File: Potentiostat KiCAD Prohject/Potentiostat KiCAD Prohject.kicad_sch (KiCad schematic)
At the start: 45 parts, among them J2 USB_C_Receptacle_USB2.0, K1 DIPxx-1Axx-12xD, SW1 Reset, SW2 Boot, U1 OPA2277, U10 ADS1115IDGS, U11 MCP4725xxx-xCH, U13 LD1117S33TR_SOT223, U14 ESP32-S2-SOLO, U2 TL074, U4 OPA2277, U5 INA128, U6 MCP4725xxx-xCH, U7 INA128, U8 REF3033, U9 INA128

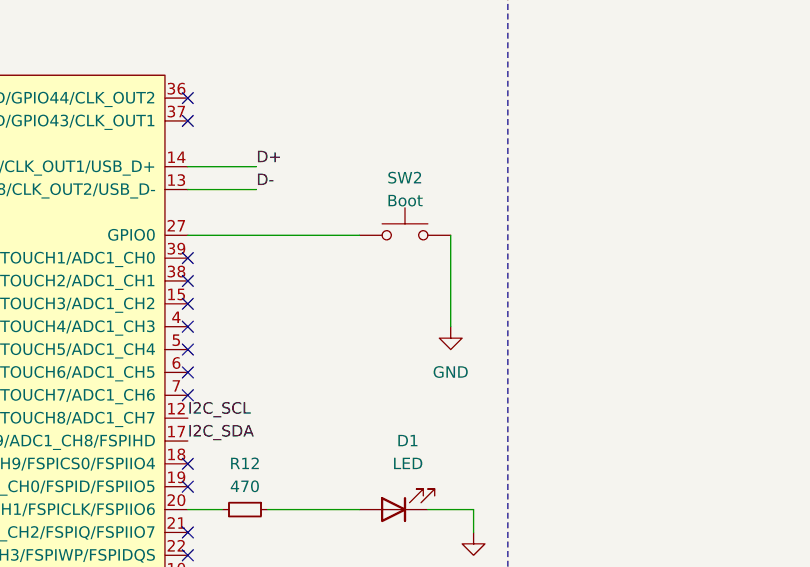
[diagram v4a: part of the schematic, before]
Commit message: Changed resistors and assigned footprints
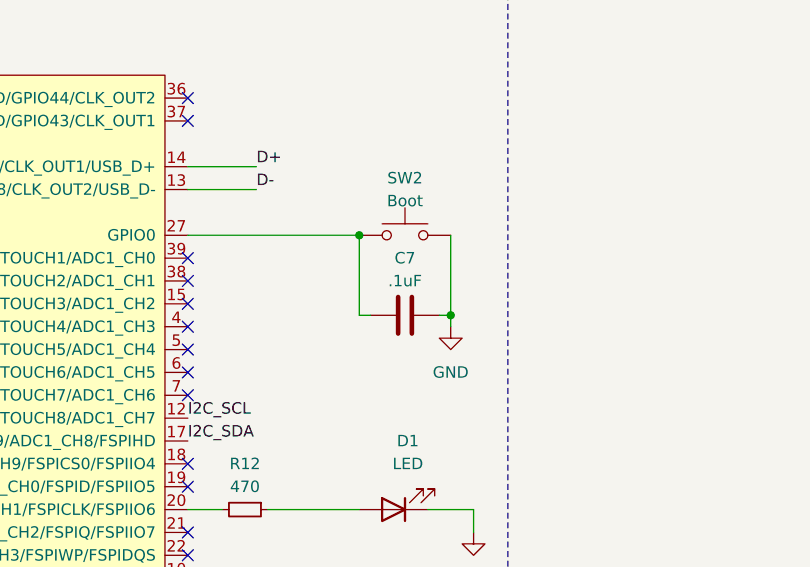
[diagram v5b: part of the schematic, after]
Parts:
- added C7: .1uF, Capacitor_SMD:C_0603_1608Metric, symbol Device:C
- C2, C3, C4, C5, C6: footprint Capacitor_SMD:C_0805_2012Metric_Pad1.18x1.45mm_HandSolder -> Capacitor_SMD:C_0603_1608Metric
- R1, R10, R11, R13, R14, R15, R16, R17, R18, R2, R3, R4, R5, R6, R7, R8, R9: footprint Resistor_THT:R_Axial_DIN0207_L6.3mm_D2.5mm_P7.62mm_Horizontal -> Resistor_SMD:R_0603_1608Metric
- R12: footprint footprints:res2_1-1625885-7_TEC -> Resistor_SMD:R_0603_1608Metric
- R19, R20, R21: footprint Resistor_SMD:R_0805_2012Metric_Pad1.20x1.40mm_HandSolder -> Resistor_SMD:R_0603_1608Metric
- SW1, SW2: footprint (none) -> Button_Switch_SMD:SW_Push_1P1T-SH_NO_CK_KMR2xxG
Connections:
- net GND: now also C7.2
- net at SW2.1, U14.27 (GPIO0): now also C7.1
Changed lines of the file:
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@@
 	)
 	(junction
+		(at 219.71 60.96)
+		(diameter 0)
+		(color 0 0 0 0)
+	)
+	(junction
 		(at 391.16 269.24)
 		(diameter 0)
@@
 	)
 	(junction
+		(at 229.87 69.85)
+		(diameter 0)
+		(color 0 0 0 0)
+	)
+	(junction
 		(at 408.94 168.91)
 		(diameter 0)
@@
 	(wire
 		(pts
+			(xy 228.6 69.85) (xy 229.87 69.85)
+		)
+		(stroke
+			(width 0)
+			(type default)
+		)
+	)
+	(wire
+		(pts
 			(xy 383.54 300.99) (xy 383.54 307.34)
 		)
@@
 	(wire
 		(pts
+			(xy 229.87 69.85) (xy 229.87 71.12)
+		)
+		(stroke
+			(width 0)
+			(type default)
+		)
+	)
+	(wire
+		(pts
 			(xy 477.52 163.83) (xy 495.3 163.83)
 		)
@@
 	(wire
 		(pts
+			(xy 220.98 69.85) (xy 219.71 69.85)
+		)
+		(stroke
+			(width 0)
+			(type default)
+		)
+	)
+	(wire
+		(pts
 			(xy 383.54 181.61) (xy 383.54 139.7)
 		)
@@
 	(wire
 		(pts
-			(xy 229.87 60.96) (xy 229.87 71.12)
+			(xy 229.87 60.96) (xy 229.87 69.85)
 		)
 		(stroke
@@
 	(wire
 		(pts
+			(xy 219.71 60.96) (xy 219.71 69.85)
+		)
+		(stroke
+			(width 0)
+			(type default)
+		)
+	)
+	(wire
+		(pts
 			(xy 213.36 189.23) (xy 190.5 189.23)
 		)
@@
 			)
 		)
-		(property "Footprint" "Resistor_THT:R_Axial_DIN0207_L6.3mm_D2.5mm_P7.62mm_Horizontal"
+		(property "Footprint" "Resistor_SMD:R_0603_1608Metric"
 			(at 455.93 288.29 0)
 			(effects
@@
 			)
 		)
-		(property "Footprint" "footprints:res2_1-1625885-7_TEC"
+		(property "Footprint" "Resistor_SMD:R_0603_1608Metric"
 			(at 207.01 91.44 0)
 			(effects
@@
 			)
 		)
-		(property "Footprint" "Resistor_THT:R_Axial_DIN0207_L6.3mm_D2.5mm_P7.62mm_Horizontal"
+		(property "Footprint" "Resistor_SMD:R_0603_1608Metric"
 			(at 410.21 276.86 0)
 			(effects
@@
 			)
 		)
-		(property "Footprint" "Resistor_THT:R_Axial_DIN0207_L6.3mm_D2.5mm_P7.62mm_Horizontal"
+		(property "Footprint" "Resistor_SMD:R_0603_1608Metric"
 			(at 393.7 293.37 0)
 			(effects
@@
 			)
 		)
-		(property "Footprint" "Resistor_SMD:R_0805_2012Metric_Pad1.20x1.40mm_HandSolder"
+		(property "Footprint" "Resistor_SMD:R_0603_1608Metric"
 			(at 96.012 39.37 90)
 			(effects
@@
 			)
 		)
-		(property "Footprint" "Capacitor_SMD:C_0805_2012Metric_Pad1.18x1.45mm_HandSolder"
+		(property "Footprint" "Capacitor_SMD:C_0603_1608Metric"
 			(at 121.6152 35.56 0)
 			(effects
@@
 			)
 		)
-		(property "Footprint" ""
+		(property "Footprint" "Button_Switch_SMD:SW_Push_1P1T-SH_NO_CK_KMR2xxG"
 			(at 224.79 55.88 0)
 			(effects
@@
 			)
 		)
-		(property "Footprint" "Resistor_THT:R_Axial_DIN0207_L6.3mm_D2.5mm_P7.62mm_Horizontal"
+		(property "Footprint" "Resistor_SMD:R_0603_1608Metric"
 			(at 264.16 160.02 0)
 			(effects
@@
 			)
 		)
-		(property "Footprint" "Capacitor_SMD:C_0805_2012Metric_Pad1.18x1.45mm_HandSolder"
+		(property "Footprint" "Capacitor_SMD:C_0603_1608Metric"
 			(at 30.1752 124.46 0)
 			(effects
@@
 			)
 		)
-		(property "Footprint" "Resistor_SMD:R_0805_2012Metric_Pad1.20x1.40mm_HandSolder"
+		(property "Footprint" "Resistor_SMD:R_0603_1608Metric"
 			(at 59.69 33.528 90)
 			(effects
@@
 			)
 		)
-		(property "Footprint" "Resistor_SMD:R_0805_2012Metric_Pad1.20x1.40mm_HandSolder"
+		(property "Footprint" "Resistor_SMD:R_0603_1608Metric"
 			(at 59.69 38.862 90)
 			(effects
@@
 			)
 		)
-		(property "Footprint" "Resistor_THT:R_Axial_DIN0207_L6.3mm_D2.5mm_P7.62mm_Horizontal"
+		(property "Footprint" "Resistor_SMD:R_0603_1608Metric"
 			(at 383.54 271.018 90)
 			(effects
@@
 			)
 		)
-		(property "Footprint" "Resistor_THT:R_Axial_DIN0207_L6.3mm_D2.5mm_P7.62mm_Horizontal"
+		(property "Footprint" "Resistor_SMD:R_0603_1608Metric"
 			(at 314.96 173.99 0)
 			(effects
@@
 			)
 		)
-		(property "Footprint" "Resistor_THT:R_Axial_DIN0207_L6.3mm_D2.5mm_P7.62mm_Horizontal"
+		(property "Footprint" "Resistor_SMD:R_0603_1608Metric"
 			(at 392.43 147.32 0)
 			(effects
@@
 			)
 		)
-		(property "Footprint" "Resistor_THT:R_Axial_DIN0207_L6.3mm_D2.5mm_P7.62mm_Horizontal"
+		(property "Footprint" "Resistor_SMD:R_0603_1608Metric"
 			(at 314.96 165.1 0)
 			(effects
@@
 			)
 		)
-		(property "Footprint" "Capacitor_SMD:C_0805_2012Metric_Pad1.18x1.45mm_HandSolder"
+		(property "Footprint" "Capacitor_SMD:C_0603_1608Metric"
 			(at 92.71 53.6448 0)
 			(effects
@@
 			)
 		)
-		(property "Footprint" "Resistor_THT:R_Axial_DIN0207_L6.3mm_D2.5mm_P7.62mm_Horizontal"
+		(property "Footprint" "Resistor_SMD:R_0603_1608Metric"
 			(at 383.54 263.398 90)
 			(effects
@@
 			)
 		)
-		(property "Footprint" "Capacitor_SMD:C_0805_2012Metric_Pad1.18x1.45mm_HandSolder"
+		(property "Footprint" "Capacitor_SMD:C_0603_1608Metric"
 			(at 134.3152 35.56 0)
 			(effects
@@
 			)
 		)
-		(property "Footprint" ""
+		(property "Footprint" "Button_Switch_SMD:SW_Push_1P1T-SH_NO_CK_KMR2xxG"
 			(at 88.9 40.64 0)
 			(effects
@@
 			)
 		)
-		(property "Footprint" "Resistor_THT:R_Axial_DIN0207_L6.3mm_D2.5mm_P7.62mm_Horizontal"
+		(property "Footprint" "Resistor_SMD:R_0603_1608Metric"
 			(at 427.99 293.37 0)
 			(effects
@@
 			)
 		)
-		(property "Footprint" "Resistor_THT:R_Axial_DIN0207_L6.3mm_D2.5mm_P7.62mm_Horizontal"
+		(property "Footprint" "Resistor_SMD:R_0603_1608Metric"
 			(at 346.71 288.29 0)
 			(effects
@@
 			)
 		)
-		(property "Footprint" "Resistor_THT:R_Axial_DIN0207_L6.3mm_D2.5mm_P7.62mm_Horizontal"
+		(property "Footprint" "Resistor_SMD:R_0603_1608Metric"
 			(at 347.98 171.45 0)
 			(effects
@@
 			)
 		)
-		(property "Footprint" "Resistor_THT:R_Axial_DIN0207_L6.3mm_D2.5mm_P7.62mm_Horizontal"
+		(property "Footprint" "Resistor_SMD:R_0603_1608Metric"
 			(at 410.21 292.1 0)
 			(effects
@@
 			)
 		)
-		(property "Footprint" "Capacitor_SMD:C_0805_2012Metric_Pad1.18x1.45mm_HandSolder"
+		(property "Footprint" "Capacitor_SMD:C_0603_1608Metric"
 			(at 63.1952 124.46 0)
 			(effects
@@
 			)
 		)
-		(property "Footprint" "Resistor_THT:R_Axial_DIN0207_L6.3mm_D2.5mm_P7.62mm_Horizontal"
+		(property "Footprint" "Resistor_SMD:R_0603_1608Metric"
 			(at 392.43 139.7 0)
 			(effects
@@
 	)
 	(symbol
+		(lib_id "Device:C")
+		(at 224.79 69.85 90)
+		(unit 1)
+		(exclude_from_sim no)
+		(in_bom yes)
+		(on_board yes)
+		(dnp no)
+		(fields_autoplaced yes)
+		(property "Reference" "C7"
+			(at 224.79 63.5 90)
+			(effects
+				(font
+					(size 1.27 1.27)
+				)
+			)
+		)
+		(property "Value" ".1uF"
+			(at 224.79 66.04 90)
+			(effects
+				(font
+					(size 1.27 1.27)
+				)
+			)
+		)
+		(property "Footprint" "Capacitor_SMD:C_0603_1608Metric"
+			(at 228.6 68.8848 0)
+			(effects
+				(font
+					(size 1.27 1.27)
+				)
+				(hide yes)
+			)
+		)
+		(property "Datasheet" "~"
+			(at 224.79 69.85 0)
+			(effects
+				(font
+					(size 1.27 1.27)
+				)
+				(hide yes)
+			)
+		)
+		(property "Description" ""
+			(at 224.79 69.85 0)
+			(effects
+				(font
+					(size 1.27 1.27)
+				)
+			)
+		)
+		(pin "1"
+		)
+		(pin "2"
+		)
+		(instances
+			(project "Potentiostat KiCAD Prohject"
+				(path "/8af48e5e-159e-4779-a191-f11ba6d6b813"
+					(reference "C7")
+					(unit 1)
+				)
+			)
+		)
+	)
+	(symbol
 		(lib_id "Device:R_Small")
 		(at 314.96 161.29 90)
@@
 			)
 		)
-		(property "Footprint" "Resistor_THT:R_Axial_DIN0207_L6.3mm_D2.5mm_P7.62mm_Horizontal"
+		(property "Footprint" "Resistor_SMD:R_0603_1608Metric"
 			(at 314.96 161.29 0)
 			(effects
@@
 			)
 		)
-		(property "Footprint" "Resistor_THT:R_Axial_DIN0207_L6.3mm_D2.5mm_P7.62mm_Horizontal"
+		(property "Footprint" "Resistor_SMD:R_0603_1608Metric"
 			(at 250.19 170.18 0)
 			(effects
@@
 			)
 		)
-		(property "Footprint" "Resistor_THT:R_Axial_DIN0207_L6.3mm_D2.5mm_P7.62mm_Horizontal"
+		(property "Footprint" "Resistor_SMD:R_0603_1608Metric"
 			(at 410.21 288.29 0)
 			(effects

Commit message: Redid layout with ground traces
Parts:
- U14: footprint PCM_Espressif:ESP32-S2-SOLO -> ESP32:ESP32-S2-SOLO
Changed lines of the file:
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@@
 			)
 		)
-		(property "Footprint" "PCM_Espressif:ESP32-S2-SOLO"
+		(property "Footprint" "ESP32:ESP32-S2-SOLO"
 			(at 154.94 137.16 0)
 			(effects

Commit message: we're so back
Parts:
- added J1, J3: Conn_01x02_Pin, Connector_PinHeader_2.54mm:PinHeader_1x02_P2.54mm_Vertical, symbol Connector:Conn_01x02_Pin
- added J4: Reference Electrode, i made this:CONN_575-8_KEY, symbol Connector:Conn_01x01_Socket
- added J5, J6: Working Electrode, i made this:CONN_575-8_KEY, symbol Connector:Conn_01x01_Socket
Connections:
- net +9V: now also J1.1 (Pin_1)
- net -9V: now also J3.2 (Pin_2)
- net GND: now also U10.1 (ADDR), J1.2 (Pin_2), J3.1 (Pin_1)
- net Reference Electrode: no longer names the net of U2.12 (+)
- net Reference Electrode: now also J4.1 (Pin_1)
- net Working Electrode: no longer names the net of K1.13, K1.2
- net Working Electrode: now also J5.1 (Pin_1); no longer U5.2 (-)
- new net: J6.1 (Pin_1), U5.2 (-)
- no-connect marks 47 -> 46
